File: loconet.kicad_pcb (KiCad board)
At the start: 2 copper layers, 79.4 x 91.6 mm, 51 parts, among them CON1 BARREL_JACK, J1 RJ12, J2 RJ12, J3 RJ12, J4 RJ12, J5 RJ12, J6 RJ12, P1 CONN_01X04, P10 CONN_01X04, P2 CONN_01X04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

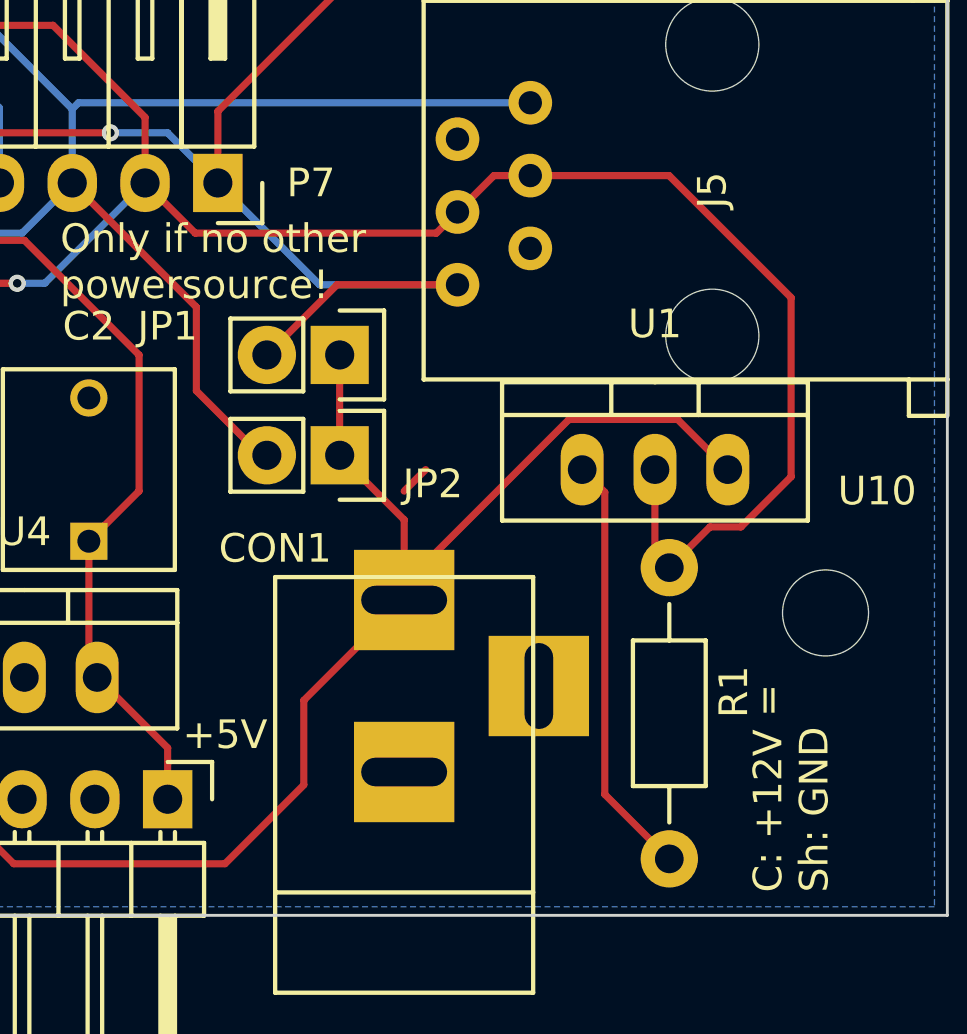
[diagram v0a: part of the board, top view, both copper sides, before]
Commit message: Fixed the "pull-up" on the loconet line
It was taken from the wrong pin of the LM317
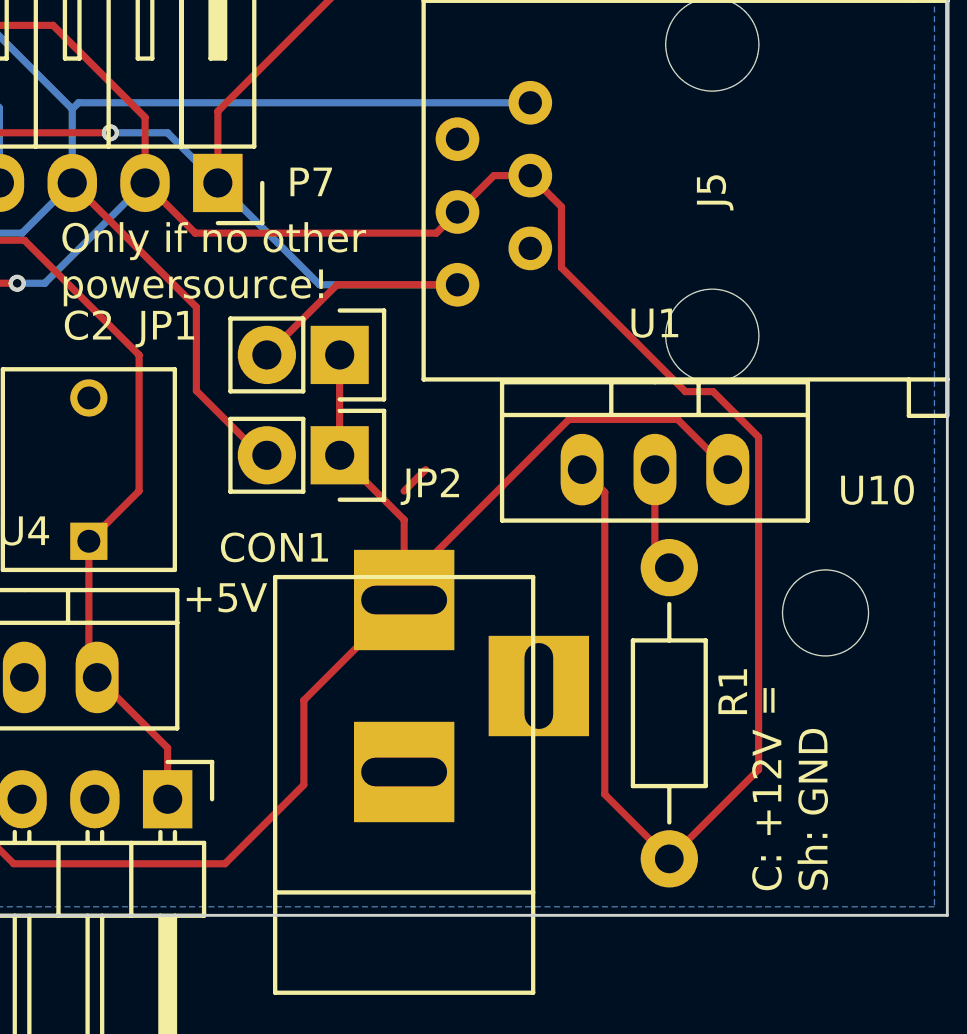
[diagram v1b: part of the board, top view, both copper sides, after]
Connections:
- R1 pad 1: Loconet -> Net-(R1-Pad1)
- R1 pad 2: Net-(R1-Pad2) -> Loconet
- U1 pad 1: Net-(R1-Pad2) -> Loconet
- U1 pad 2: Loconet -> Net-(R1-Pad1)
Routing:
- net Loconet: track 297.4 -> 314.9 mm
- net Net-(R1-Pad2): track 14.8 -> 0.00 mm
- net Net-(R1-Pad1): track 0.00 -> 3.63 mm
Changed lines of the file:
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@@
-(kicad_pcb (version 4) (host pcbnew "(2015-05-08 BZR 5647)-product")
+(kicad_pcb (version 4) (host pcbnew "(2015-08-02 BZR 6038)-product")
   (general
     (links 104)
-    (no_connects 0)
-    (area 99.899999 58.515 200.100001 160.100001)
+    (no_connects 1)
+    (area 113.949999 60.949999 193.500001 152.600001)
     (thickness 1.6)
     (drawings 51)
-    (tracks 279)
+    (tracks 281)
     (zones 0)
     (modules 51)
@@
   (net 12 "Net-(U2-Pad6)")
   (net 13 +12V)
-  (net 14 "Net-(R1-Pad2)")
+  (net 14 "Net-(R1-Pad1)")
   (net_class Default "This is the default net class."
     (clearance 0.2)
@@
     (add_net Loconet_TX)
     (add_net "Net-(Q1-Pad2)")
-    (add_net "Net-(R1-Pad2)")
+    (add_net "Net-(R1-Pad1)")
     (add_net "Net-(R2-Pad2)")
     (add_net "Net-(R4-Pad2)")
@@
     (fp_line (start 2.54 0) (end 3.81 0) (layer F.SilkS) (width 0.15))
     (pad 1 thru_hole circle (at -5.08 0 270) (size 1.99898 1.99898) (drill 1.00076) (layers *.Cu *.SilkS *.Mask)
-      (net 1 Loconet))
+      (net 14 "Net-(R1-Pad1)"))
     (pad 2 thru_hole circle (at 5.08 0 270) (size 1.99898 1.99898) (drill 1.00076) (layers *.Cu *.SilkS *.Mask)
-      (net 14 "Net-(R1-Pad2)"))
+      (net 1 Loconet))
     (model Resistors_ThroughHole.3dshapes/Resistor_Horizontal_RM10mm.wrl
       (at (xyz 0 0 0))
@@
     (fp_line (start 0 -3.048) (end 5.334 -3.048) (layer F.SilkS) (width 0.15))
     (pad 2 thru_hole oval (at 0 0 90) (size 2.49936 1.50114) (drill 1.00076) (layers *.Cu *.Mask F.SilkS)
-      (net 1 Loconet))
+      (net 14 "Net-(R1-Pad1)"))
     (pad 1 thru_hole oval (at -2.54 0 90) (size 2.49936 1.50114) (drill 1.00076) (layers *.Cu *.Mask F.SilkS)
-      (net 14 "Net-(R1-Pad2)"))
+      (net 1 Loconet))
     (pad 3 thru_hole oval (at 2.54 0 90) (size 2.49936 1.50114) (drill 1.00076) (layers *.Cu *.Mask F.SilkS)
       (net 13 +12V))
@@
     (effects (font (size 1 1) (thickness 0.15)))
   )
-  (gr_text "+5V\n" (at 168.25 146.25) (layer F.SilkS)
+  (gr_text "+5V\n" (at 168.25 141.5) (layer F.SilkS)
     (effects (font (size 1 1) (thickness 0.15)))
   )
@@
   (segment (start 174.5 137.75) (end 175.25 137) (width 0.25) (layer F.Cu) (net 0))
   (segment (start 167.64 75.67) (end 167.695 75.67) (width 0.25) (layer F.Cu) (net 0) (status 30))
+  (segment (start 183.75 150.58) (end 186.86558 147.46442) (width 0.25) (layer F.Cu) (net 1))
+  (segment (start 185.280001 134.280001) (end 184.313999 134.280001) (width 0.25) (layer F.Cu) (net 1))
+  (segment (start 186.86558 147.46442) (end 186.86558 135.86558) (width 0.25) (layer F.Cu) (net 1))
+  (segment (start 179.987001 129.953003) (end 179.987001 127.829001) (width 0.25) (layer F.Cu) (net 1))
+  (segment (start 179.661999 127.503999) (end 178.9 126.742) (width 0.25) (layer F.Cu) (net 1))
+  (segment (start 186.86558 135.86558) (end 185.280001 134.280001) (width 0.25) (layer F.Cu) (net 1))
+  (segment (start 184.313999 134.280001) (end 179.987001 129.953003) (width 0.25) (layer F.Cu) (net 1))
+  (segment (start 179.987001 127.829001) (end 179.661999 127.503999) (width 0.25) (layer F.Cu) (net 1))
   (segment (start 176.36 102.762) (end 175.138 101.54) (width 0.25) (layer F.Cu) (net 1))
   (segment (start 175.138 101.54) (end 165.46 101.54) (width 0.25) (layer F.Cu) (net 1))
@@
   (segment (start 144.46 99) (end 144.46 112.5) (width 0.25) (layer B.Cu) (net 1))
   (segment (start 165.46 99) (end 165.46 112.5) (width 0.25) (layer F.Cu) (net 1))
-  (segment (start 183.25 139.92) (end 183.25 137) (width 0.25) (layer F.Cu) (net 1))
-  (segment (start 183.75 140.42) (end 183.25 139.92) (width 0.25) (layer F.Cu) (net 1))
-  (segment (start 185.17 139) (end 186.25 139) (width 0.25) (layer F.Cu) (net 1))
-  (segment (start 186.25 139) (end 188 137.25) (width 0.25) (layer F.Cu) (net 1))
-  (segment (start 188 137.25) (end 188 131) (width 0.25) (layer F.Cu) (net 1))
-  (segment (start 188 131) (end 183.742 126.742) (width 0.25) (layer F.Cu) (net 1))
-  (segment (start 183.742 126.742) (end 178.9 126.742) (width 0.25) (layer F.Cu) (net 1))
-  (segment (start 183.75 140.42) (end 185.17 139) (width 0.25) (layer F.Cu) (net 1))
   (segment (start 142.71 128.75) (end 139 128.75) (width 0.25) (layer F.Cu) (net 1))
   (segment (start 139 128.75) (end 137 130.75) (width 0.25) (layer F.Cu) (net 1))
@@
   (segment (start 161.96 130.5) (end 165.46 127) (width 0.25) (layer B.Cu) (net 1))
   (segment (start 149 148.83) (end 154 143.83) (width 0.25) (layer F.Cu) (net 1))
+  (segment (start 181.5 148.33) (end 181.5 137.79) (width 0.25) (layer F.Cu) (net 1))
+  (segment (start 181.5 137.79) (end 180.71 137) (width 0.25) (layer F.Cu) (net 1))
+  (segment (start 183.75 150.58) (end 181.5 148.33) (width 0.25) (layer F.Cu) (net 1))
   (segment (start 178.9 106.6) (end 178.9 104.032) (width 0.25) (layer B.Cu) (net 2))
   (segment (start 175.5 110) (end 178.9 106.6) (width 0.25) (layer B.Cu) (net 2))
@@
   (segment (start 174.5 141.54986) (end 174.5 138.75) (width 0.25) (layer F.Cu) (net 13))
   (segment (start 172.25 136.5) (end 172.25 133) (width 0.25) (layer F.Cu) (net 13))
-  (segment (start 181.5 148.33) (end 181.5 137.79) (width 0.25) (layer F.Cu) (net 14))
-  (segment (start 181.5 137.79) (end 180.71 137) (width 0.25) (layer F.Cu) (net 14))
-  (segment (start 183.75 150.58) (end 181.5 148.33) (width 0.25) (layer F.Cu) (net 14))
+  (segment (start 183.25 139.92) (end 183.25 137) (width 0.25) (layer F.Cu) (net 14))
+  (segment (start 183.75 140.42) (end 183.25 139.92) (width 0.25) (layer F.Cu) (net 14))
   (zone (net 2) (net_name GND) (layer B.Cu) (hatch edge 0.508)
     (connect_pads (clearance 0.508))

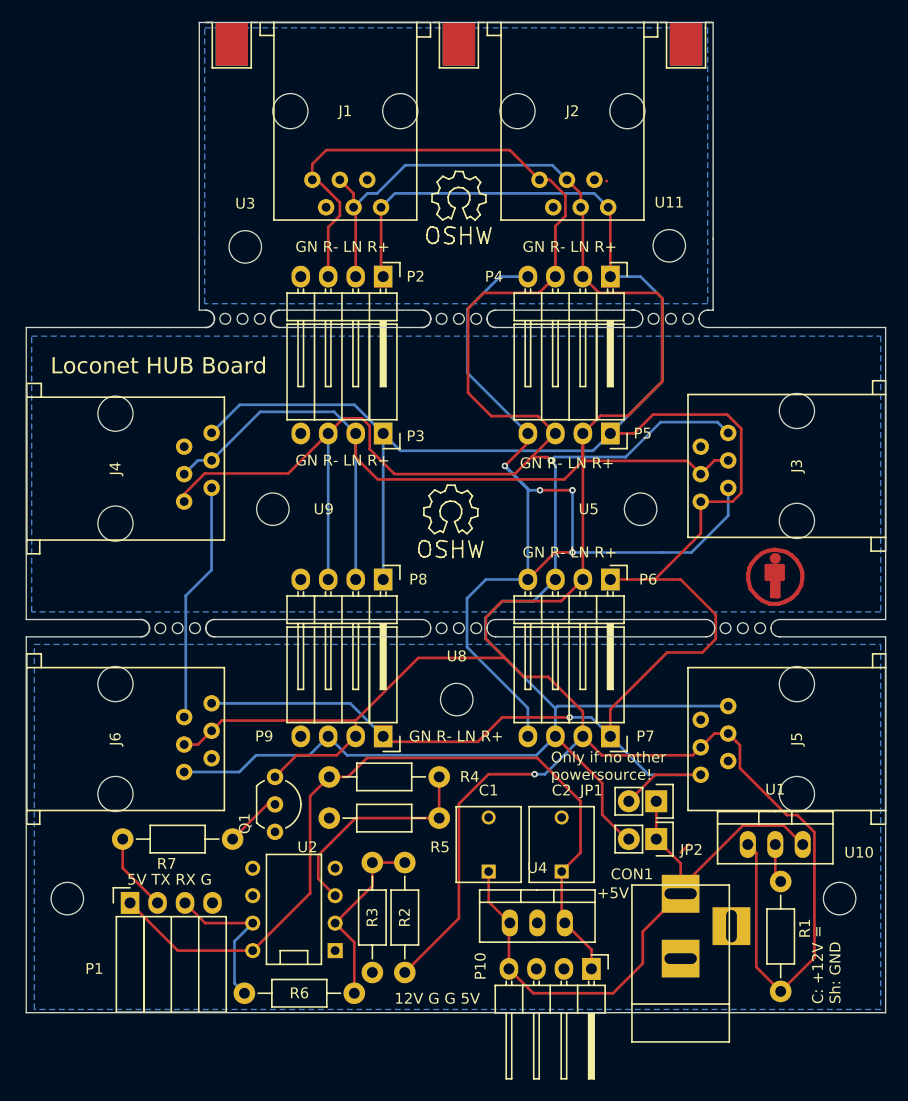
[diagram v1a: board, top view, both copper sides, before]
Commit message: Updated footprints to 4.0.7 standards
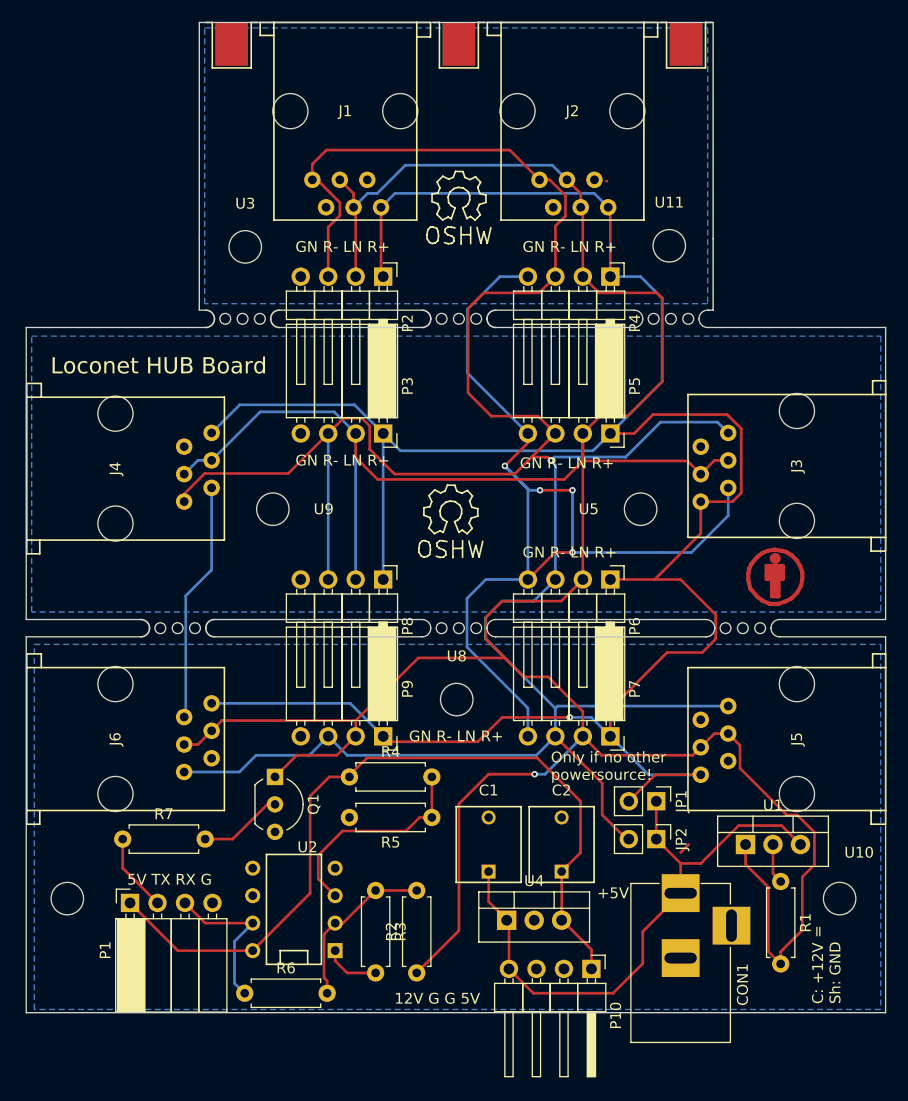
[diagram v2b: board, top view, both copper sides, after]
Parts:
- CON1: footprint Connect:BARREL_JACK -> Connectors:BARREL_JACK
- JP1, JP2: footprint Pin_Headers:Pin_Header_Straight_1x02 -> Pin_Headers:Pin_Header_Straight_1x02_Pitch2.54mm
- P1, P3, P5, P7, P9: footprint Socket_Strips:Socket_Strip_Angled_1x04 -> Socket_Strips:Socket_Strip_Angled_1x04_Pitch2.54mm
- P10, P2, P4, P6, P8: footprint Pin_Headers:Pin_Header_Angled_1x04 -> Pin_Headers:Pin_Header_Angled_1x04_Pitch2.54mm
- Q1: footprint Housings_TO-92:TO-92_Inline_Wide -> TO_SOT_Packages_THT:TO-92_Inline_Wide
- R1, R2, R3, R4, R5, R6, R7: footprint Resistors_ThroughHole:Resistor_Horizontal_RM10mm -> Resistors_THT:R_Axial_DIN0207_L6.3mm_D2.5mm_P7.62mm_Horizontal
- U1, U4: footprint Transistors_TO-220:TO-220_Neutral123_Vertical -> TO_SOT_Packages_THT:TO-220_Vertical
- moved CON1 6.25 mm to (174.5, 141.5)
- moved R2 5.24 mm to (150.1, 148.9)
- moved R1 5.08 mm to (183.8, 140.4)
- moved R7 5.08 mm to (122.9, 136.5)
- moved R6 5.05 mm to (134.2, 150.8)
- moved R5 4.40 mm to (151.5, 134.5)
- moved R4 3.22 mm to (143.9, 130.8)
- moved U4 2.84 mm to (158.4, 144.0)
- moved U1 2.75 mm to (180.5, 137.0)
- moved R3 2.52 mm to (146.3, 141.2)
- turned P1 to 90 degrees
- turned P3 to 270 degrees
- turned P5 to 270 degrees
- turned P7 to 270 degrees
- turned P9 to 270 degrees
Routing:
- net Loconet: track 314.9 -> 309.5 mm
- net GND: track 116.0 -> 121.2 mm
- net Net-(Q1-Pad2): track 5.25 -> 7.79 mm
- net Net-(R2-Pad2): track 17.2 -> 15.8 mm
- net +12V: track 56.5 -> 55.4 mm
- net Net-(R4-Pad2): track 20.8 -> 20.1 mm
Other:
- outline, holes or cut-outs redrawn
